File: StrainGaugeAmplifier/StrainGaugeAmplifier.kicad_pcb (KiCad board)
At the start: 2 copper layers, 140 x 50 mm, 44 parts, among them K1 BS-115C-12A-12VDC, X1 WF-4, X2 WF-5, X3 WF-6, X4 WF-3

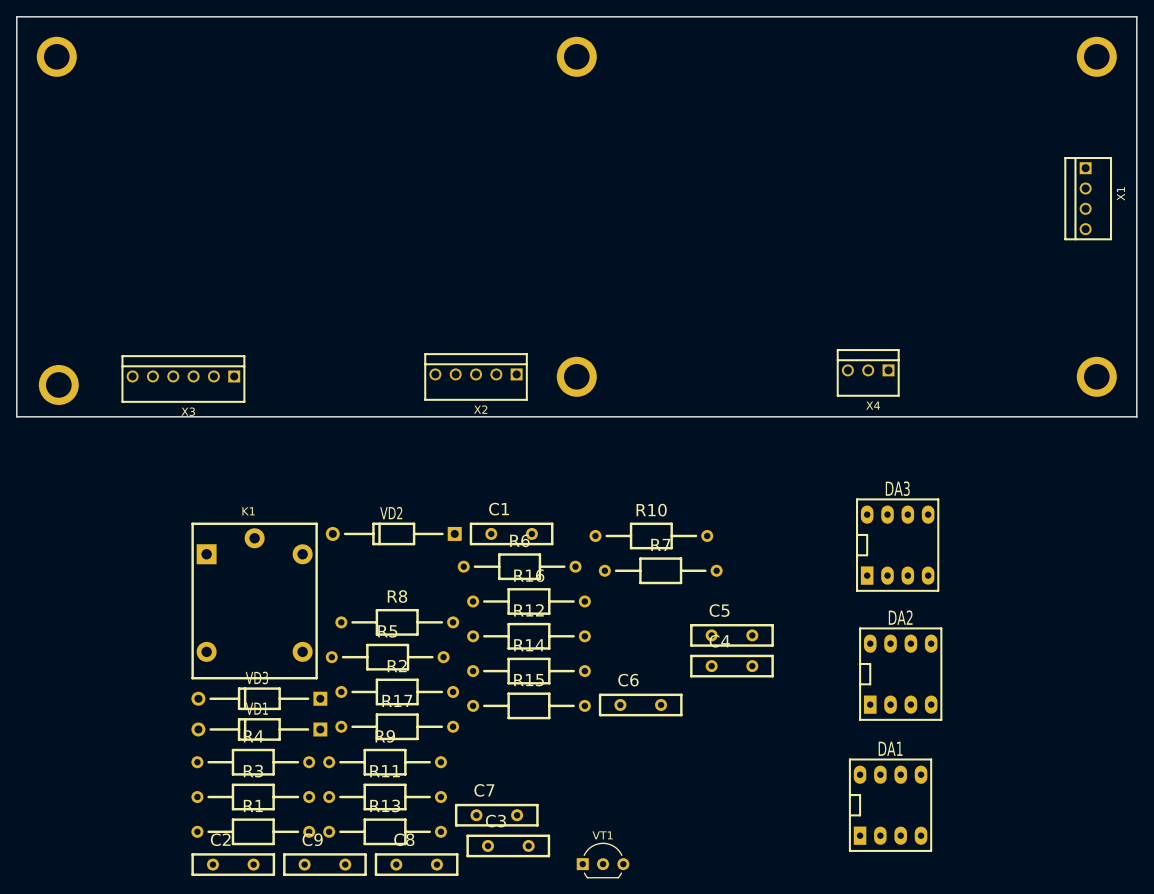
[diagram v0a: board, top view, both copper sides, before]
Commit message: Расположил элементы на плате и повёл трассировку.
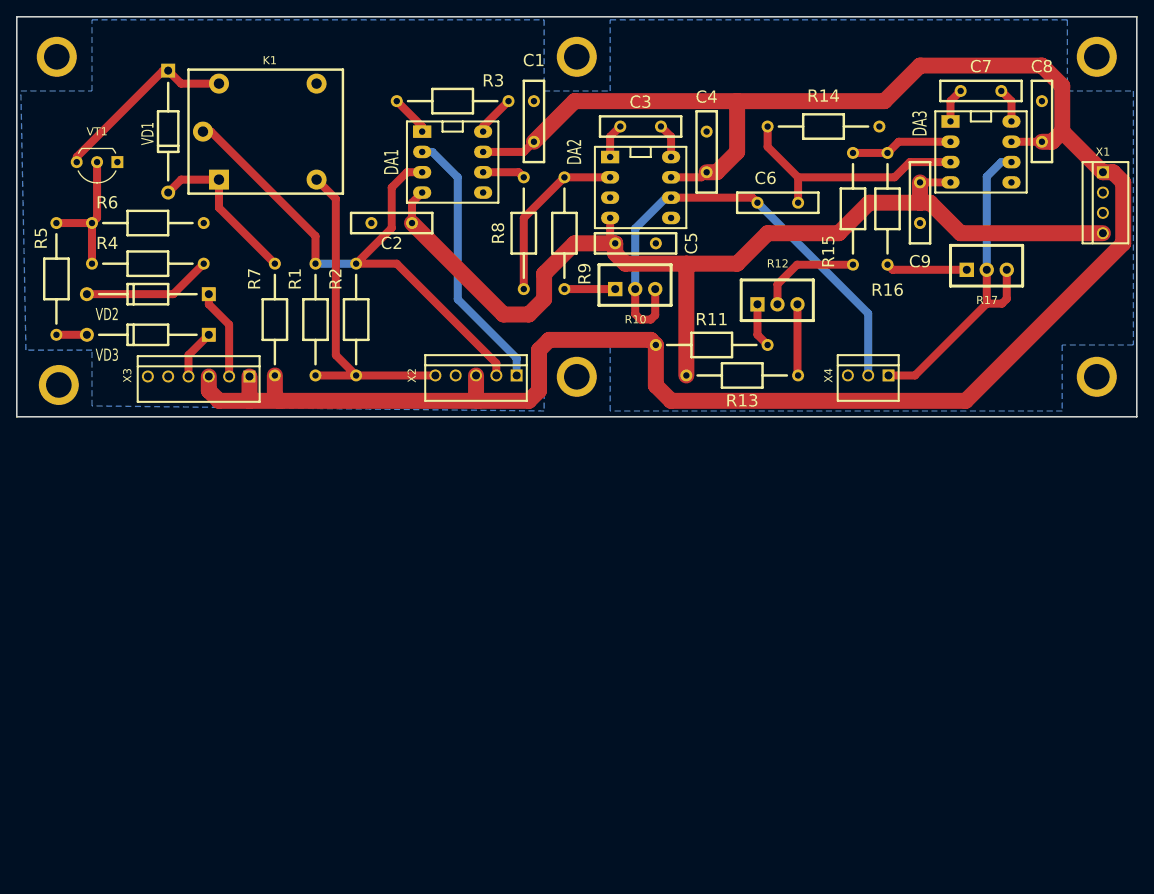
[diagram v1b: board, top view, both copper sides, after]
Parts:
- R10, R12, R17: footprint IWcomponents:RESISTOR_0.25W -> IWcomponents:Electron_3296W
- moved C8 121.4 mm to (205.7, 73.7), turned to 90 degrees
- moved C9 111.3 mm to (190.5, 83.8), turned to 270 degrees
- moved C7 108.9 mm to (198.1, 69.8), turned to 180 degrees
- moved VT1 105.3 mm to (90.2, 78.7), turned to 180 degrees
- moved DA1 97.3 mm to (132.1, 78.7), turned to 270 degrees
- moved C3 91.4 mm to (155.6, 74.3), turned to 180 degrees
- moved R17 91.3 mm to (196.3, 92.2)
- moved R3 90.5 mm to (132.1, 71.1), turned to 180 degrees
- moved C2 82.6 mm to (124.5, 86.4), turned to 180 degrees
- moved R14 77.4 mm to (178.4, 74.3), turned to 180 degrees
- moved R15 74.2 mm to (182.1, 84.6), turned to 270 degrees
- moved R13 72.4 mm to (168.3, 105.4), turned to 180 degrees
- moved R9 69.8 mm to (146.1, 87.6), turned to 90 degrees
- moved R11 69.7 mm to (164.5, 101.6)
- moved DA2 69.0 mm to (155.6, 81.9), turned to 270 degrees
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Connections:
- DA3 pad 6: Net-(DA3-Pad5) -> Net-(DA3-Pad6)
- R17 pad 2: Net-(DA3-Pad5) -> Net-(DA3-Pad6)
- X2 pad 1: Net-(DA1-Pad3) -> Net-(DA1-Pad2)
- X2 pad 2: Net-(DA1-Pad2) -> Net-(DA1-Pad3)
- X4 pad 1: Net-(DA3-Pad5) -> Net-(DA3-Pad6)
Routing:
- net /+VCC: track 0.00 -> 271.1 mm
- net /-VCC: track 0.00 -> 131.3 mm
- net Net-(DA1-Pad3): track 0.00 -> 68.9 mm
- net Net-(C6-Pad1): track 0.00 -> 61.4 mm
- net Net-(DA3-Pad6): track 0.00 -> 42.1 mm
- net Net-(K1-Pad5): track 0.00 -> 41.8 mm
- net Net-(DA1-Pad2): track 0.00 -> 33.6 mm
- net Net-(C6-Pad2): track 0.00 -> 30.9 mm
- net Net-(K1-Pad8): track 0.00 -> 23.6 mm
- net Net-(DA2-Pad2): track 0.00 -> 21.8 mm
- net Net-(K1-Pad1): track 0.00 -> 20.7 mm
- net Net-(R4-Pad1): track 0.00 -> 17.4 mm
- net Net-(R4-Pad2): track 0.00 -> 16.2 mm
- net Net-(R12-Pad2): track 0.00 -> 13.0 mm
- net Net-(DA3-Pad2): track 0.00 -> 12.8 mm
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- added copper zone on B.Cu, net /GND

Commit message: Отправил печатные платы в производство.
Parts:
- moved 1_PIN 1.02 mm to (82.9, 105.6)
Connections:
- R1 pad 2: Net-(K1-Pad5) -> Net-(K1-Pad7)
- R2 pad 2: Net-(K1-Pad5) -> Net-(K1-Pad7)
- X2 pad 5: Net-(K1-Pad5) -> Net-(K1-Pad7)
- X3 pad 3: /+VCC -> /GND
- X3 pad 4: Net-(VD3-Pad1) -> /+VCC
- X3 pad 5: Net-(X3-Pad5) -> Net-(VD3-Pad1)
- X3 pad 6: Net-(X3-Pad6) -> /GND
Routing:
- net Net-(K1-Pad7): track 0.00 -> 53.5 mm
- net Net-(K1-Pad5): track 41.8 -> 0.26 mm
- net /+VCC: track 271.1 -> 273.8 mm
- net Net-(VD3-Pad1): track 6.26 -> 8.06 mm
